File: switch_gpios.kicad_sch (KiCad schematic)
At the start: 0 parts

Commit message: CuPhy: adding ports
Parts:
- added U1: ~, Package_QFP:TQFP-128_14x14mm_P0.4mm, symbol lan9645xF:lan9645xF_128_TQFP

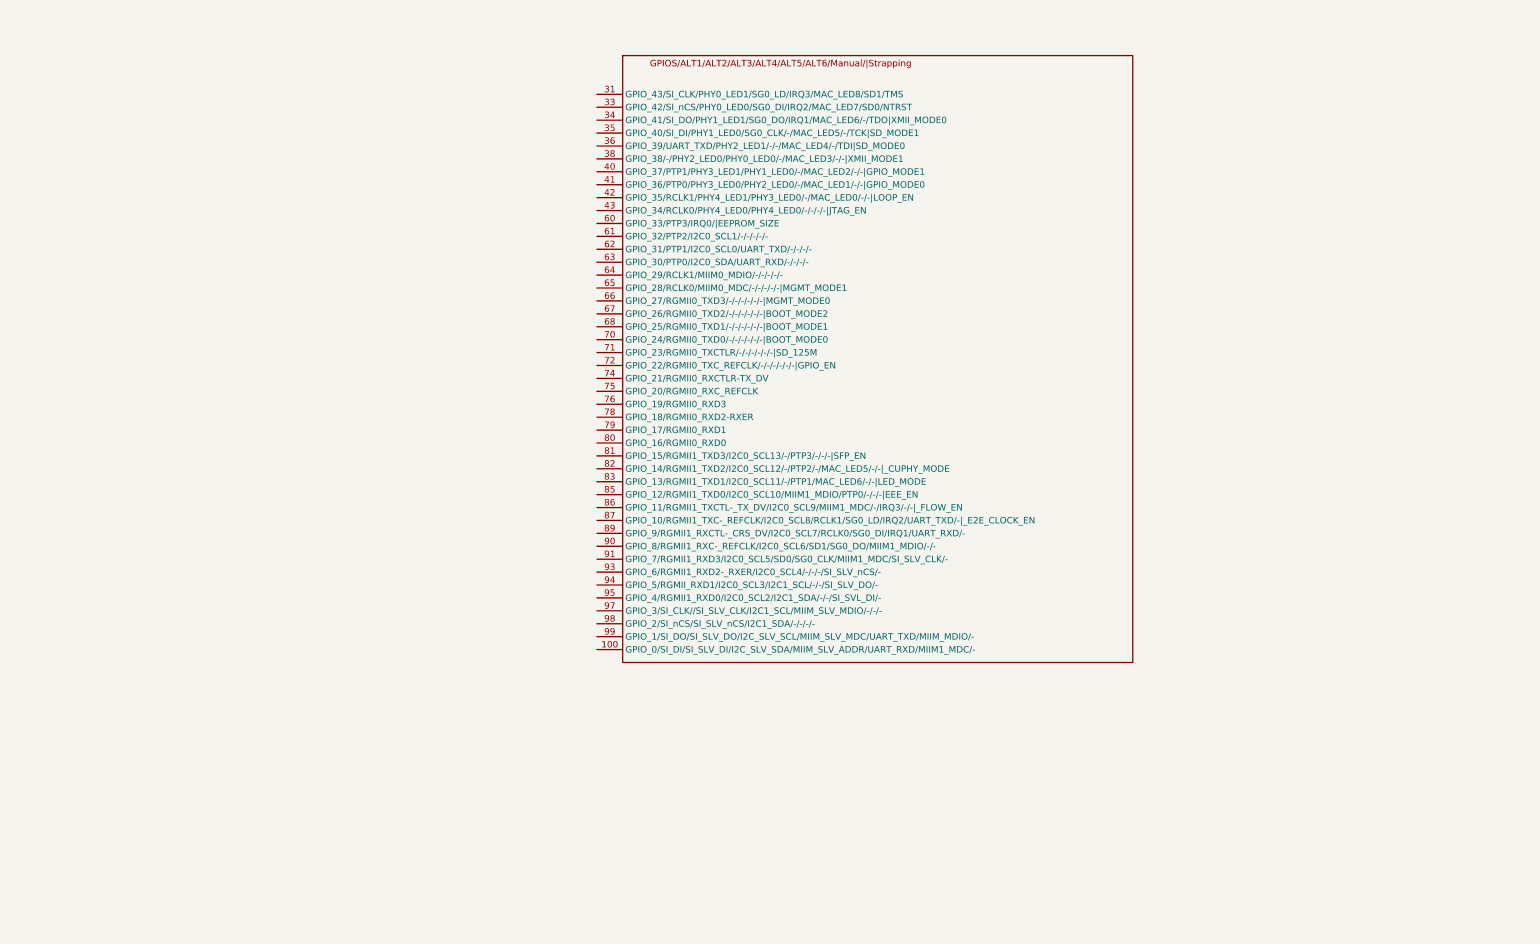
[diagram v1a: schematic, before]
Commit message: gpios: first version of the GPIOS and strapping schematics
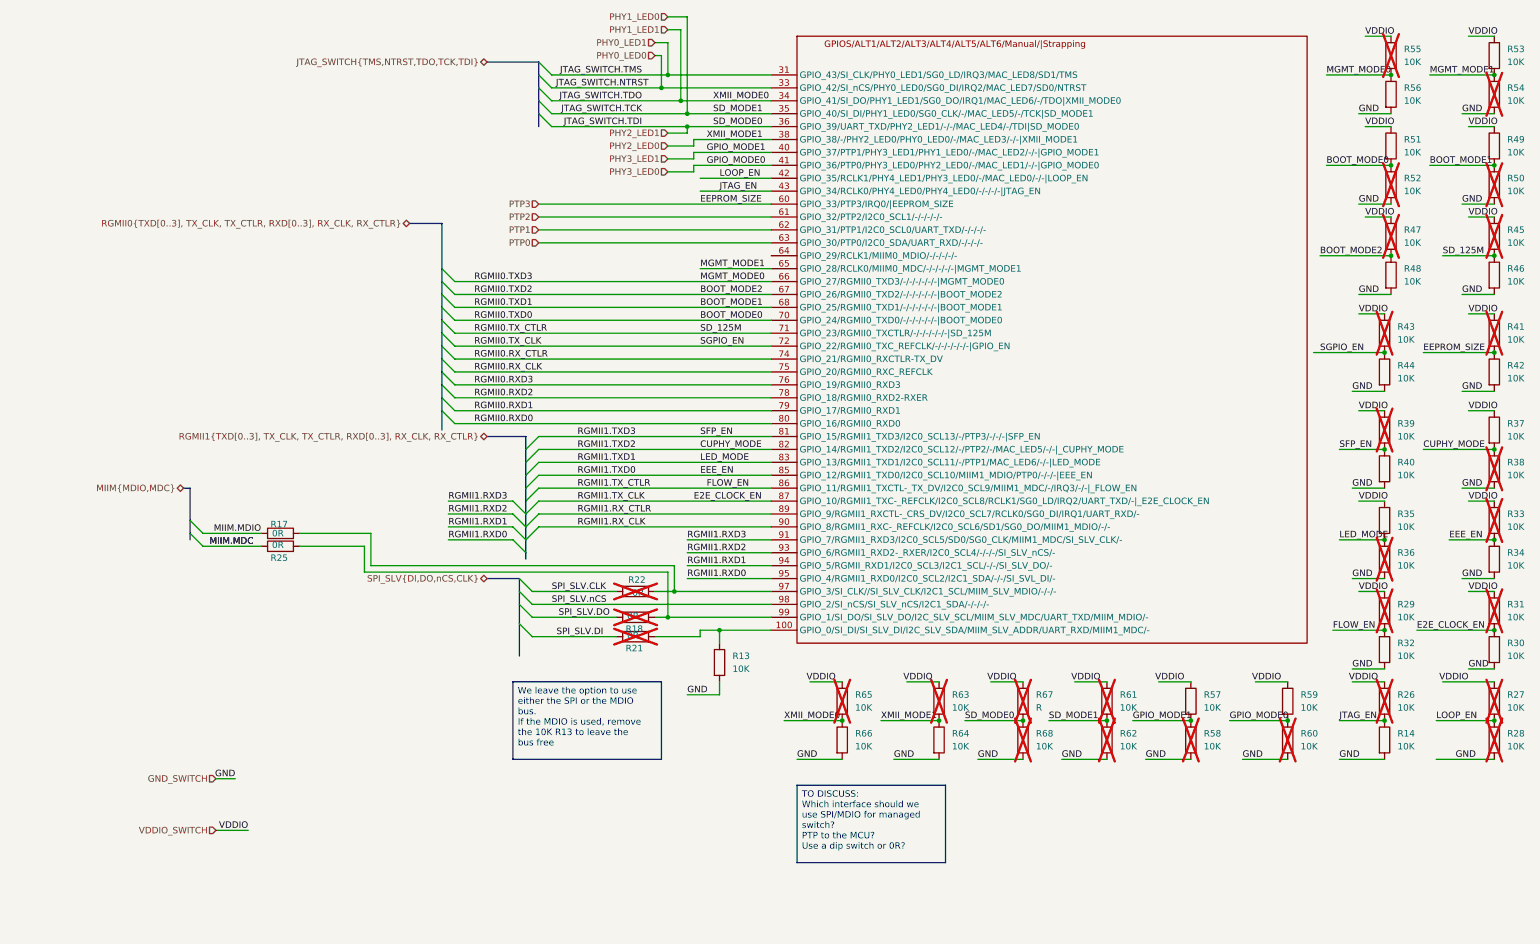
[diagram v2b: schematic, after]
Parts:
- added R13, R14, R26, R27, R28, R29, R30, R31, R32, R33, R34, R35, R36, R37, R38, R39, R40, R41, R42, R43, R44, R45, R46, R47, R48, R49, R50, R51, R52, R53, R54, R55, R56, R57, R58, R59, R60, R61, R62, R63, R64, R65, R66, R68: 10K, symbol Device:R
- added R17, R18, R21, R22, R25: 0R, symbol Device:R
- added R67: R, symbol Device:R
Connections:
- net at U1.100 (GPIO_0/SI_DI/SI_SLV_DI/I2C_SLV_SDA/MIIM_SLV_ADDR/UART_RXD/MIIM1_MDC/-): now also R13.1, R21.2
- net PHY0_LED1: now reaches U1.31 (GPIO_43/SI_CLK/PHY0_LED1/SG0_LD/IRQ3/MAC_LED8/SD1/TMS)
- net PHY0_LED0: now reaches U1.33 (GPIO_42/SI_nCS/PHY0_LED0/SG0_DI/IRQ2/MAC_LED7/SD0/NTRST)
- net PHY1_LED1: now reaches U1.34 (GPIO_41/SI_DO/PHY1_LED1/SG0_DO/IRQ1/MAC_LED6/-/TDO|XMII_MODE0)
- net PHY1_LED1: now also R65.2, R66.1
- net PHY1_LED0: now reaches U1.35 (GPIO_40/SI_DI/PHY1_LED0/SG0_CLK/-/MAC_LED5/-/TCK|SD_MODE1)
- net PHY1_LED0: now also R61.2, R62.1
- net PHY2_LED1: now reaches U1.36 (GPIO_39/UART_TXD/PHY2_LED1/-/-/MAC_LED4/-/TDI|SD_MODE0)
- net PHY2_LED1: now also R67.2, R68.1
- net PHY2_LED0: now reaches U1.38 (GPIO_38/-/PHY2_LED0/PHY0_LED0/-/MAC_LED3/-/-|XMII_MODE1)
- net PHY2_LED0: now also R63.2, R64.1
- net PHY3_LED1: now reaches U1.40 (GPIO_37/PTP1/PHY3_LED1/PHY1_LED0/-/MAC_LED2/-/-|GPIO_MODE1)
- net PHY3_LED1: now also R57.2, R58.1
- net PHY3_LED0: now reaches U1.41 (GPIO_36/PTP0/PHY3_LED0/PHY2_LED0/-/MAC_LED1/-/-|GPIO_MODE0)
- net PHY3_LED0: now also R59.2, R60.1
- net LOOP_EN: now reaches U1.42 (GPIO_35/RCLK1/PHY4_LED1/PHY3_LED0/-/MAC_LED0/-/-|LOOP_EN)
- net LOOP_EN: now also R27.2, R28.1
- net JTAG_EN: now reaches U1.43 (GPIO_34/RCLK0/PHY4_LED0/PHY4_LED0/-/-/-/-|JTAG_EN)
- net JTAG_EN: now also R14.1, R26.2
- net PTP3: now reaches U1.60 (GPIO_33/PTP3/IRQ0/|EEPROM_SIZE)
- net PTP3: now also R41.2, R42.1
- net PTP2: now reaches U1.61 (GPIO_32/PTP2/I2C0_SCL1/-/-/-/-/-)
- net PTP1: now reaches U1.62 (GPIO_31/PTP1/I2C0_SCL0/UART_TXD/-/-/-/-)
- net PTP0: now reaches U1.63 (GPIO_30/PTP0/I2C0_SDA/UART_RXD/-/-/-/-)
- net MGMT_MODE1: now reaches U1.65 (GPIO_28/RCLK0/MIIM0_MDC/-/-/-/-/-|MGMT_MODE1)
- net MGMT_MODE1: now also R53.2, R54.1
- net MGMT_MODE0: now reaches U1.66 (GPIO_27/RGMII0_TXD3/-/-/-/-/-/-|MGMT_MODE0)
- net MGMT_MODE0: now also R55.2, R56.1
- net BOOT_MODE2: now reaches U1.67 (GPIO_26/RGMII0_TXD2/-/-/-/-/-/-|BOOT_MODE2)
- net BOOT_MODE2: now also R47.2, R48.1
- net BOOT_MODE1: now reaches U1.68 (GPIO_25/RGMII0_TXD1/-/-/-/-/-/-|BOOT_MODE1)
- net BOOT_MODE1: now also R49.2, R50.1
- net BOOT_MODE0: now reaches U1.70 (GPIO_24/RGMII0_TXD0/-/-/-/-/-/-|BOOT_MODE0)
- net BOOT_MODE0: now also R51.2, R52.1
- net RGMII0.TX_CTLR: now reaches U1.71 (GPIO_23/RGMII0_TXCTLR/-/-/-/-/-/-|SD_125M)
- net RGMII0.TX_CTLR: now also R45.2, R46.1
- net RGMII0.TX_CLK: now reaches U1.72 (GPIO_22/RGMII0_TXC_REFCLK/-/-/-/-/-/-|GPIO_EN)
- net RGMII0.TX_CLK: now also R43.2, R44.1
- net RGMII0.RX_CTLR: now reaches U1.74 (GPIO_21/RGMII0_RXCTLR-TX_DV)
- net RGMII0.RX_CLK: now reaches U1.75 (GPIO_20/RGMII0_RXC_REFCLK)
- net RGMII0.RXD3: now reaches U1.76 (GPIO_19/RGMII0_RXD3)
- net RGMII0.RXD2: now reaches U1.78 (GPIO_18/RGMII0_RXD2-RXER)
- net RGMII0.RXD1: now reaches U1.79 (GPIO_17/RGMII0_RXD1)
- net RGMII0.RXD0: now reaches U1.80 (GPIO_16/RGMII0_RXD0)
- net RGMII1.TXD3: now reaches U1.81 (GPIO_15/RGMII1_TXD3/I2C0_SCL13/-/PTP3/-/-/-|SFP_EN)
- net RGMII1.TXD3: now also R39.2, R40.1
- net CUPHY_MODE: now reaches U1.82 (GPIO_14/RGMII1_TXD2/I2C0_SCL12/-/PTP2/-/MAC_LED5/-/-|_CUPHY_MODE)
- net CUPHY_MODE: now also R37.2, R38.1
- net LED_MODE: now reaches U1.83 (GPIO_13/RGMII1_TXD1/I2C0_SCL11/-/PTP1/MAC_LED6/-/-|LED_MODE)
- net LED_MODE: now also R35.2, R36.1
- net EEE_EN: now reaches U1.85 (GPIO_12/RGMII1_TXD0/I2C0_SCL10/MIIM1_MDIO/PTP0/-/-/-|EEE_EN)
- net EEE_EN: now also R33.2, R34.1
- net FLOW_EN: now reaches U1.86 (GPIO_11/RGMII1_TXCTL-_TX_DV/I2C0_SCL9/MIIM1_MDC/-/IRQ3/-/-|_FLOW_EN)
- net FLOW_EN: now also R29.2, R32.1
- net E2E_CLOCK_EN: now reaches U1.87 (GPIO_10/RGMII1_TXC-_REFCLK/I2C0_SCL8/RCLK1/SG0_LD/IRQ2/UART_TXD/-|_E2E_CLOCK_EN)
- net E2E_CLOCK_EN: now also R30.1, R31.2
- net RGMII1.RX_CTLR: now reaches U1.89 (GPIO_9/RGMII1_RXCTL-_CRS_DV/I2C0_SCL7/RCLK0/SG0_DI/IRQ1/UART_RXD/-)
- net RGMII1.RX_CLK: now reaches U1.90 (GPIO_8/RGMII1_RXC-_REFCLK/I2C0_SCL6/SD1/SG0_DO/MIIM1_MDIO/-/-)
- net RGMII1.RXD3: now reaches U1.91 (GPIO_7/RGMII1_RXD3/I2C0_SCL5/SD0/SG0_CLK/MIIM1_MDC/SI_SLV_CLK/-)
- net RGMII1.RXD2: now reaches U1.93 (GPIO_6/RGMII1_RXD2-_RXER/I2C0_SCL4/-/-/-/SI_SLV_nCS/-)
- net RGMII1.RXD1: now reaches U1.94 (GPIO_5/RGMII_RXD1/I2C0_SCL3/I2C1_SCL/-/-/SI_SLV_DO/-)
- net RGMII1.RXD0: now reaches U1.95 (GPIO_4/RGMII1_RXD0/I2C0_SCL2/I2C1_SDA/-/-/SI_SVL_DI/-)
- net at U1.97 (GPIO_3/SI_CLK//SI_SLV_CLK/I2C1_SCL/MIIM_SLV_MDIO/-/-/-): now also R17.2, R22.1
- net SPI_SLV.nCS: now reaches U1.98 (GPIO_2/SI_nCS/SI_SLV_nCS/I2C1_SDA/-/-/-/-)
- net at U1.99 (GPIO_1/SI_DO/SI_SLV_DO/I2C_SLV_SCL/MIIM_SLV_MDC/UART_TXD/MIIM_MDIO/-): now also R18.2, R25.2
- new net GND_SWITCH: R13.2, R14.2, R28.2, R30.2, R32.2, R34.2, R36.2, R38.2, R40.2, R42.2, R44.2, R46.2, R48.2, R50.2, R52.2, R54.2, R56.2, R58.2, R60.2, R62.2, R64.2, R66.2, R68.2
- new net MIIM.MDC: R25.1
- new net MIIM.MDIO: R17.1
- new net SPI_SLV.CLK: R22.2
- new net SPI_SLV.DI: R21.1
- new net SPI_SLV.DO: R18.1
- new net VDDIO_SWITCH: R26.1, R27.1, R29.1, R31.1, R33.1, R35.1, R37.1, R39.1, R41.1, R43.1, R45.1, R47.1, R49.1, R51.1, R53.1, R55.1, R57.1, R59.1, R61.1, R63.1, R65.1, R67.1
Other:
- title: (none) -> Switch GPIOs and Strapping

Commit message: schematics: fixing the voltage rail and updating the files
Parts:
- added R69: 4.7K, symbol Device:R
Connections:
- net VDDIO_SWITCH: now also R69.2
- net at R17.2, R22.1, U1.97 (GPIO_3/SI_CLK//SI_SLV_CLK/I2C1_SCL/MIIM_SLV_MDIO/-/-/-): now also R69.1
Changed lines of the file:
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@@
 	)
 	(junction
+		(at 52.07 115.57)
+		(diameter 0)
+		(color 0 0 0 0)
+	)
+	(junction
 		(at 259.08 43.18)
 		(diameter 0)
@@
 	(wire
 		(pts
-			(xy 44.45 115.57) (xy 58.42 115.57)
+			(xy 44.45 115.57) (xy 52.07 115.57)
 		)
 		(stroke
@@
 		)
 	)
+	(wire
+		(pts
+			(xy 45.72 107.95) (xy 52.07 107.95)
+		)
+		(stroke
+			(width 0)
+			(type default)
+		)
+	)
 	(bus
 		(pts
@@
 	(wire
 		(pts
+			(xy 52.07 115.57) (xy 58.42 115.57)
+		)
+		(stroke
+			(width 0)
+			(type default)
+		)
+	)
+	(wire
+		(pts
 			(xy 254 17.78) (xy 259.08 17.78)
 		)
@@
 		)
 	)
+	(label "VDDIO"
+		(at 45.72 107.95 0)
+		(effects
+			(font
+				(size 1.27 1.27)
+			)
+			(justify left bottom)
+		)
+	)
 	(label "SPI_SLV.DI"
 		(at 104.14 135.89 180)
@@
 	)
 	(hierarchical_label "PTP0"
-		(shape input)
+		(shape bidirectional)
 		(at 91.44 58.42 180)
 		(effects
@@
 	)
 	(hierarchical_label "PTP2"
-		(shape input)
+		(shape bidirectional)
 		(at 91.44 53.34 180)
 		(effects
@@
 	)
 	(hierarchical_label "PTP3"
-		(shape input)
+		(shape bidirectional)
 		(at 91.44 50.8 180)
 		(effects
@@
 	)
 	(hierarchical_label "PHY2_LED0"
-		(shape input)
+		(shape output)
 		(at 116.84 39.37 180)
 		(effects
@@
 	)
 	(hierarchical_label "PHY3_LED0"
-		(shape input)
+		(shape output)
 		(at 116.84 44.45 180)
 		(effects
@@
 	)
 	(hierarchical_label "PHY3_LED1"
-		(shape input)
+		(shape output)
 		(at 116.84 41.91 180)
 		(effects
@@
 	)
 	(hierarchical_label "PHY2_LED1"
-		(shape input)
+		(shape output)
 		(at 116.84 36.83 180)
 		(effects
@@
 	)
 	(hierarchical_label "PHY1_LED0"
-		(shape input)
+		(shape output)
 		(at 116.84 13.97 180)
 		(effects
@@
 	)
 	(hierarchical_label "PHY0_LED1"
-		(shape input)
+		(shape output)
 		(at 114.3 19.05 180)
 		(effects
@@
 	)
 	(hierarchical_label "PHY1_LED1"
-		(shape input)
+		(shape output)
 		(at 116.84 16.51 180)
 		(effects
@@
 	)
 	(hierarchical_label "PHY0_LED0"
-		(shape input)
+		(shape output)
 		(at 114.3 21.59 180)
 		(effects
@@
 	)
 	(hierarchical_label "PTP1"
-		(shape input)
+		(shape bidirectional)
 		(at 91.44 55.88 180)
 		(effects
@@
 		)
 	)
+	(netclass_flag ""
+		(length 2.54)
+		(shape round)
+		(at 83.82 96.52 180)
+		(effects
+			(font
+				(size 1.27 1.27)
+			)
+			(justify right bottom)
+		)
+		(property "Netclass" "RGMII"
+			(at 81.788 100.838 0)
+			(effects
+				(font
+					(size 1.27 1.27)
+				)
+				(justify left)
+			)
+		)
+		(property "Component Class" ""
+			(at -99.06 26.67 0)
+			(effects
+				(font
+					(size 1.27 1.27)
+					(italic yes)
+				)
+			)
+		)
+	)
+	(netclass_flag ""
+		(length 2.54)
+		(shape round)
+		(at 69.85 54.61 0)
+		(fields_autoplaced yes)
+		(effects
+			(font
+				(size 1.27 1.27)
+			)
+			(justify left bottom)
+		)
+		(property "Netclass" "RGMII"
+			(at 70.5485 52.07 0)
+			(effects
+				(font
+					(size 1.27 1.27)
+				)
+				(justify left)
+			)
+		)
+		(property "Component Class" ""
+			(at -113.03 -15.24 0)
+			(effects
+				(font
+					(size 1.27 1.27)
+					(italic yes)
+				)
+			)
+		)
+	)
 	(symbol
 		(lib_id "Device:R")
@@
 					(unit 1)
 				)
+			)
+		)
+	)
+	(symbol
+		(lib_id "Device:R")
+		(at 52.07 111.76 180)
+		(unit 1)
+		(exclude_from_sim no)
+		(in_bom yes)
+		(on_board yes)
+		(dnp no)
+		(property "Reference" "R69"
+			(at 50.292 112.014 90)
+			(effects
+				(font
+					(size 1.27 1.27)
+				)
+			)
+		)
+		(property "Value" "4.7K"
+			(at 52.07 112.268 90)
+			(effects
+				(font
+					(size 1.27 1.27)
+				)
+			)
+		)
+		(property "Footprint" ""
+			(at 53.848 111.76 90)
+			(effects
+				(font
+					(size 1.27 1.27)
+				)
+				(hide yes)
+			)
+		)
+		(property "Datasheet" "~"
+			(at 52.07 111.76 0)
+			(effects
+				(font
+					(size 1.27 1.27)
+				)
+				(hide yes)
+			)
+		)
+		(property "Description" "Resistor"
+			(at 52.07 111.76 0)
+			(effects
+				(font
+					(size 1.27 1.27)
+				)
+				(hide yes)
+			)
+		)
+		(property "manf#" " RMCA0603FT4K70-HP"
+			(at 52.07 111.76 0)
+			(effects
+				(font
+					(size 1.27 1.27)
+				)
+				(hide yes)
+			)
+		)
+		(pin "1"
+		)
+		(pin "2"
+		)
+		(instances
+			(project "shish-lan"
+				(path "/d4536448-b109-4159-96e2-3dc21baf2d6e/0b7d9af9-83c1-43fa-a7a0-a33d0a00ea9c/7f5fd65f-f670-4db7-8f09-63d4fb2faa09"
+					(reference "R69")
+					(unit 1)
+				)
